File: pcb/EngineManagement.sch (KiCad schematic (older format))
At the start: 42 parts, among them K1 Temps, K5 FuelCool, K6 FuelCoolAlt, K7 Supply, U1 LM7808CT, U3 ArdinoMinPro, U5 MCP2515Shield

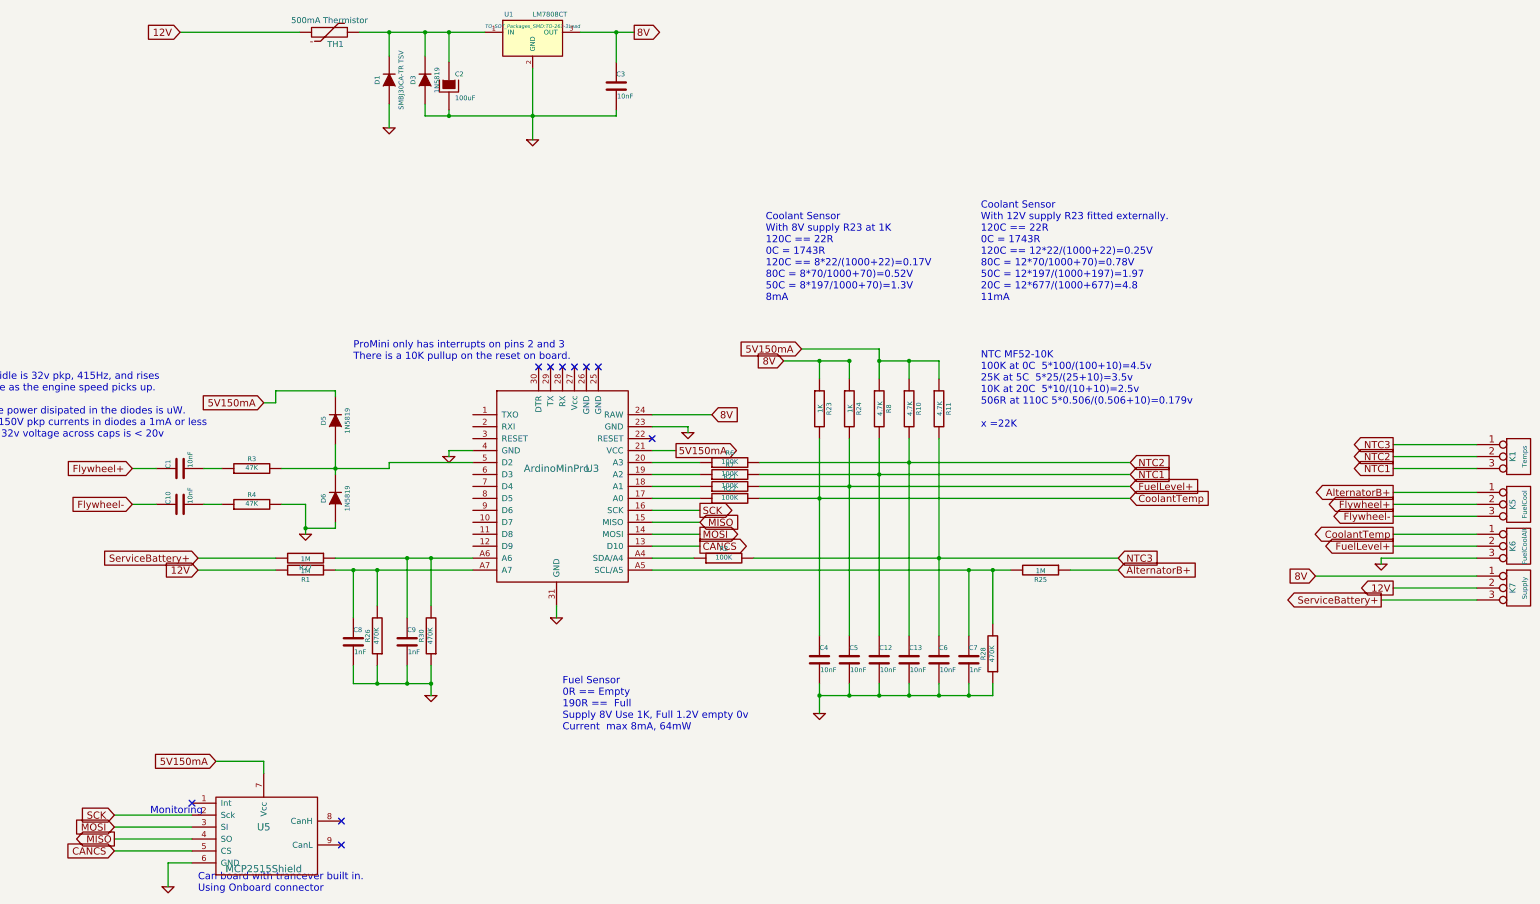
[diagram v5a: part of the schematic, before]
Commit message: Added mosfet based board
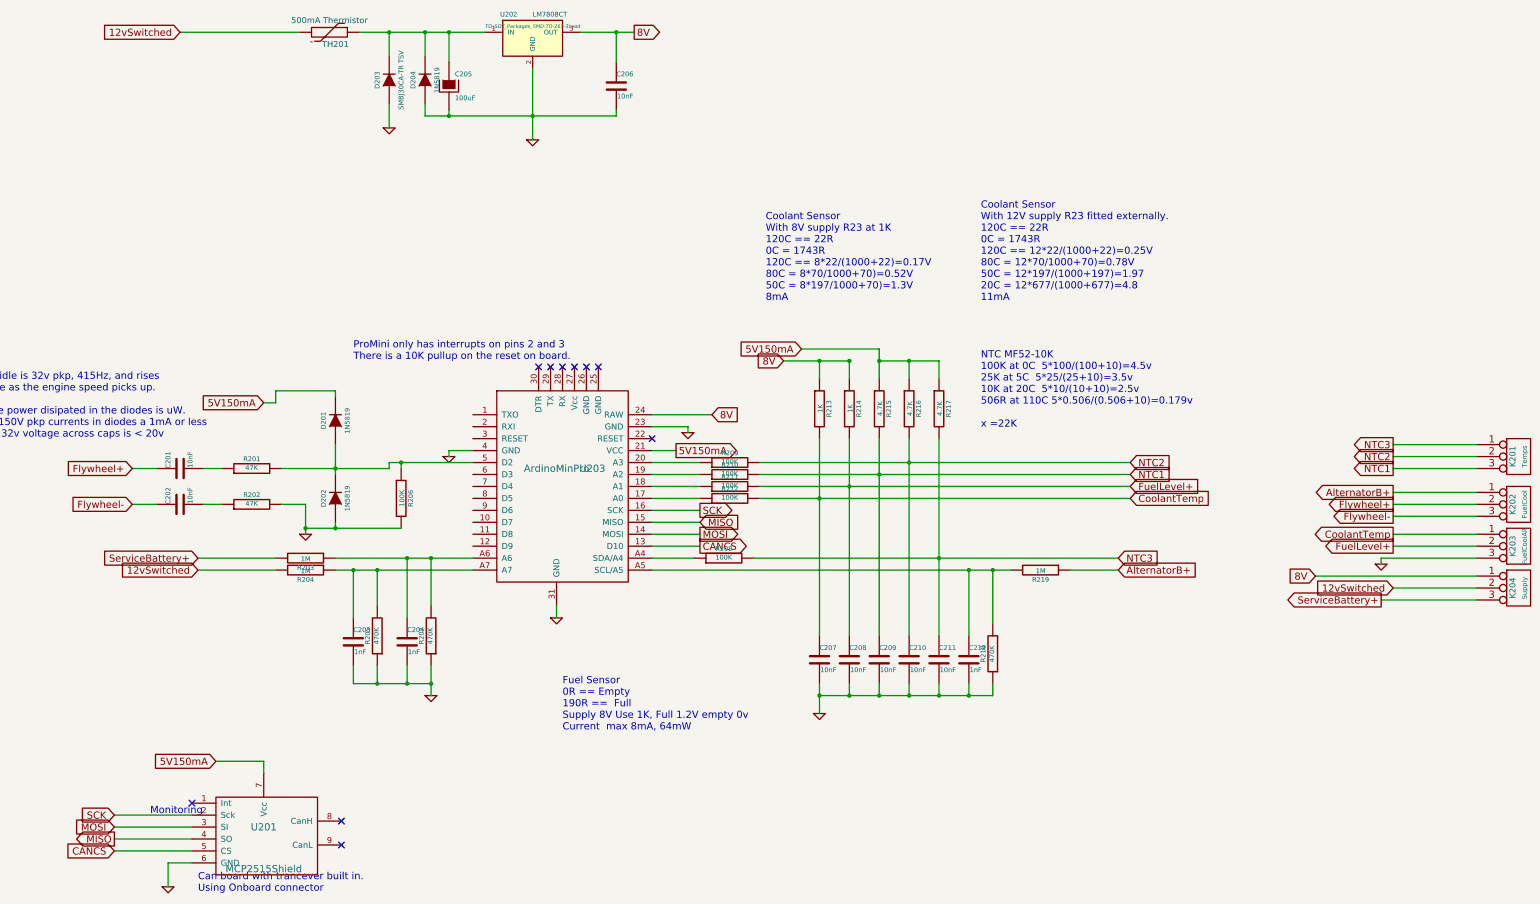
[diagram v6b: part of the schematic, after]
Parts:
- added R206: 100K, Resistors_SMD:R_0805_HandSoldering, symbol R
- D201: renamed from D5; footprint Resistors_ThroughHole:Resistor_Horizontal_RM7mm -> Diodes_SMD:SOD-123
- D202: renamed from D6; footprint Resistors_ThroughHole:Resistor_Horizontal_RM7mm -> Diodes_SMD:D_SOD-123
- D204: renamed from D3; footprint Resistors_ThroughHole:Resistor_Horizontal_RM7mm -> Diodes_SMD:D_SOD-123
- renumbered C1 to C201, C10 to C202, C8 to C203, C9 to C204, C2 to C205, C3 to C206, C4 to C207, C5 to C208, C12 to C209, C13 to C210, C6 to C211, C7 to C212, D1 to D203, K1 to K201, K5 to K202, K6 to K203, K7 to K204, R3 to R201, R4 to R202, R27 to R203, R1 to R204, R26 to R205, R30 to R207, R2 to R208, R6 to R209, R7 to R210, R21 to R211, R22 to R212, R23 to R213, R24 to R214, R8 to R215, R10 to R216, R11 to R217, R28 to R218, R25 to R219, TH1 to TH201, U5 to U201, U1 to U202, U3 to U203
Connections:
- net GND: now also R206.2
- net at D201.1 (A), D202.2 (K), R201.2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: now also R206.1
- net 12V renamed 12vSwitched

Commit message: After testing, fixed a number of things
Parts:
- added C101, C102: 22pF, Resistors_SMD:R_0603_HandSoldering, symbol C
- added C103: 10uF, Resistors_SMD:R_1206_HandSoldering, symbol C
- added C104, C105: 100nF, Capacitors_SMD:C_0805_HandSoldering, symbol C
- added D101, D102: SMBJ30CA-TR TSV, Diodes_SMD:DO-214AB_Handsoldering, symbol DIODE
- added P101: CanBus, Connect:bornier2, symbol CONN_2
- added R101: 10K, Resistors_SMD:R_0805_HandSoldering, symbol R
- added R220: 22K, Resistors_SMD:R_0805_HandSoldering, symbol R
- added R221, R222: 100K, Resistors_SMD:R_0805_HandSoldering, symbol R
- added U101: MCP2515, Housings_SOIC:SOIC-18W_7.5x11.6mm_Pitch1.27mm, symbol MCP2515
- added U102: TJA1050, Housings_SOIC:SOIC-8_3.9x4.9mm_Pitch1.27mm, symbol TJA1050
- added U204: LM358, Housings_DIP:DIP-8_W7.62mm_LongPads, symbol LM358
- added X101: 8MHz, Crystals:Resonator-2pin_w10.0mm_h5.0mm, symbol CRYSTAL
- C201, C202: value 10nF -> 1uF; footprint Capacitors_SMD:C_0805_HandSoldering -> Capacitors_SMD:C_1210
- D201: footprint Diodes_SMD:SOD-123 -> Diodes_SMD:D_SOD-123
- D204: footprint Diodes_SMD:D_SOD-123 -> Resistors_ThroughHole:Resistor_Horizontal_RM7mm
- R201, R202: value 47K -> 22K
- R206: value 100K -> 1K
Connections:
- net 5V150mA: now also C103.2, C104.2, C105.2, R101.2, U101.18 (Vdd), U102.3 (Vcc), U204.8 (V+); no longer D201.2 (K)
- net 8V: no longer K204.1 (P1)
- net CANCS: now also U101.16 (CS)
- net Flywheel+: now also R201.1; no longer C201.1
- net Flywheel-: now also R202.1; no longer C202.1
- net GND: now also C201.2, C202.2, D201.2 (K), K204.1 (P1), C101.2, C102.2, C103.1, C104.1, C105.1, D101.1 (A), D102.1 (A), R221.1, U101.9 (GND), U102.2 (GND), U102.8 (S), U204.4 (V-)
- net MISO: now also U101.15 (SO)
- net MOSI: now also U101.14 (SI)
- net SCK: now also U101.13 (SCK)
- net at D201.1 (A), D202.2 (K), R201.2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: now also C201.1, R220.2, R222.2, U204.3 (+); no longer U203.5 (D2)
- new net: C202.1, R222.1, U204.2 (-)
- new net: U101.1 (CANTX), U102.1 (TXD)
- new net: R101.1, U101.17 (RESET)
- new net: U101.2 (CANRX), U102.4 (RXD)
- new net: C102.1, U101.7 (OSC2), X101.2
- new net: C101.1, U101.8 (OSC1), X101.1
- new net: D101.2 (K), P101.2 (PM), U102.6 (CanH)
- new net: D102.2 (K), P101.1 (P1), U102.7 (CanL)
- new net RPMPulse: R220.1, R221.2, U203.5 (D2), U204.1
- no-connect marks 10 -> 18
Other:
- note added: "Flywheel or Alternator W+ Input"
- note added: "Op Amp configured as Schmitt Trigger with control over hysterisis.\nThe RC on the -Vin on the op amp automatically adjusts bias of the\ninput signal to ensure switching always occurs at the mean voltage \nof the input signal. RC is set so it take a few cycles at low frequency and perhaps 100 at KHz"
- note added: "Threshold Peak to Peak voltages to trigger square wave out.\n\n4KHz >= 80V\n3KHz >= 60V\n2KHz >= 40V\n1KHz >= 20V\n500Hz >= 13V\n400Hz >= 12V\n200Hz >= 10V"
- moved on the sheet: R201, R202, U201
